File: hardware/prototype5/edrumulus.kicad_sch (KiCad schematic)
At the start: 67 parts, among them J1 Trigger Connector, J2 Raspberry Pi GPIO pins, U1 ESP32-WROOM-32U

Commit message: some more work for prototype 5
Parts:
- removed D18, D19, D20, D22, D23, D24: BAT85, Diode_SMD:D_MiniMELF, symbol Diode:BAT85
- removed R26, R27, R28: 100 kOhm, Resistor_SMD:R_1206_3216Metric_Pad1.30x1.75mm_HandSolder, symbol pspice:R
- removed R30, R31, R32, R34, R35, R36: 22 kOhm, Resistor_SMD:R_1206_3216Metric_Pad1.30x1.75mm_HandSolder, symbol pspice:R
- added D? (x6): BAT85, Diode_SMD:D_MiniMELF, symbol Diode:BAT85
- added R? (x6): 22 kOhm, Resistor_SMD:R_1206_3216Metric_Pad1.30x1.75mm_HandSolder, symbol pspice:R
- added R? (x3): 100 kOhm, Resistor_SMD:R_1206_3216Metric_Pad1.30x1.75mm_HandSolder, symbol pspice:R
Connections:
- net 3V3: now also D?.1 (K), D?.1 (K), D?.1 (K), R?.1, R?.1, R?.1
- net CRASH1-SLEEVE: now also D?.2 (A), D?.2 (A), D?.2 (A), R?.2, R?.2, R?.2
- net GPIO12: now also D?.1 (K), D?.2 (A), R?.1, R?.1, R?.2
- net GPIO15: now also D?.1 (K), D?.2 (A), R?.1, R?.1, R?.2
- net GPIO39: now also D?.1 (K), D?.2 (A), R?.1, R?.1, R?.2
- net TOM1-TIP: now also R?.2
- net TOM2-TIP: now also R?.2
- net TOM3-TIP: now also R?.2
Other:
- moved on the sheet: D1, D10, D11, D12, D13, D14, D15, D16, D17, D2, D21, D25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

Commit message: some more work on prototype 5
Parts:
- removed D? (x2): BAT85, Diode_SMD:D_MiniMELF, symbol Diode:BAT85
- removed R? (x2): 22 kOhm, Resistor_SMD:R_1206_3216Metric_Pad1.30x1.75mm_HandSolder, symbol pspice:R
- removed R?: 100 kOhm, Resistor_SMD:R_1206_3216Metric_Pad1.30x1.75mm_HandSolder, symbol pspice:R
- added C1, C10, C11, C12, C13, C14, C15, C2, C3, C4, C5, C6, C7, C8, C9: 100 nF, symbol Device:C
- added C16: 1 µF, symbol Device:C
- added C17: 22 µF, symbol Device:C_Polarized
- added C18: 10 nF, symbol Device:C
- added C19: 10 µF, symbol Device:C_Polarized
- added D18, D19, D27, D28, D29, D30: BAT85, Diode_SMD:D_MiniMELF, symbol Diode:BAT85
- added R26, R35, R36: 100 kOhm, Resistor_SMD:R_1206_3216Metric_Pad1.30x1.75mm_HandSolder, symbol pspice:R
- added R27, R28, R41, R42, R43, R44: 22 kOhm, Resistor_SMD:R_1206_3216Metric_Pad1.30x1.75mm_HandSolder, symbol pspice:R
- added U2: AMS1117-3.3, Package_TO_SOT_SMD:SOT-223-3_TabPin2, symbol Regulator_Linear:AMS1117-3.3
- added U3: LT1761-3.3, Package_TO_SOT_SMD:TSOT-23-5, symbol Regulator_Linear:LT1761-3.3
- gave numbers to parts that had none: 10
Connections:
- net 3V3: now also C1.2, C10.2, C11.1, C12.2, C13.1, C14.2, C15.1, C18.1, C19.1, C2.1, C3.2, C4.2, C5.1, C6.2, C7.2, C8.1, C9.2, D19.1 (K), D29.1 (K), D30.1 (K), R28.1, R43.1, R44.1, U3.5 (VOUT); no longer U1.2 (VDD)
- net CRASH1-SLEEVE: now also C1.1, C10.1, C11.2, C12.1, C13.2, C14.1, C15.2, C16.2, C17.2, C19.2, C2.2, C3.1, C4.1, C5.2, C6.1, C7.1, C8.2, C9.1, D18.2 (A), D27.2 (A), D28.2 (A), R27.2, R41.2, R42.2, U2.1 (GND), U3.2 (GND)
- net GPIO39: now also D28.1 (K), D30.2 (A), R36.2, R42.1, R44.2
- net TOM1-TIP: now also R36.1
- net TOM1-RING: now reaches J1.15 (P15)
- net TOM1-RING: now also R35.1
- net RIDE-BELL-TIP: now reaches J1.25 (P25)
- net RIDE-BELL-TIP: now also R26.1
- net GPIO2: now reaches U1.24 (IO2)
- net GPIO2: now also D18.1 (K), D19.2 (A), R26.2, R27.1, R28.2
- net GPIO4: now reaches U1.26 (IO4)
- net GPIO4: now also D27.1 (K), D29.2 (A), R35.2, R41.1, R43.2
- net ESP-VIN renamed RASPI-VIN
- net RASPI-VIN: now also C16.1, U2.3 (VI), U3.1 (VIN), U3.3 (~{SHDN})
- new net: C18.2, U3.4 (BYP)
- new net ESP32-3V3: C17.1, U1.2 (VDD), U2.2 (VO)
- no-connect marks 34 -> 38
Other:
- note added: "TODO ESP 32 enable TODO Board LED"
- title: Edrumulus Prototype 4 (ESP32) -> Edrumulus Prototype 5 (ESP32)
- moved on the sheet: D17, D20, D21, D22, D23, D24, D25, D26, J1, J2, R25, R29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

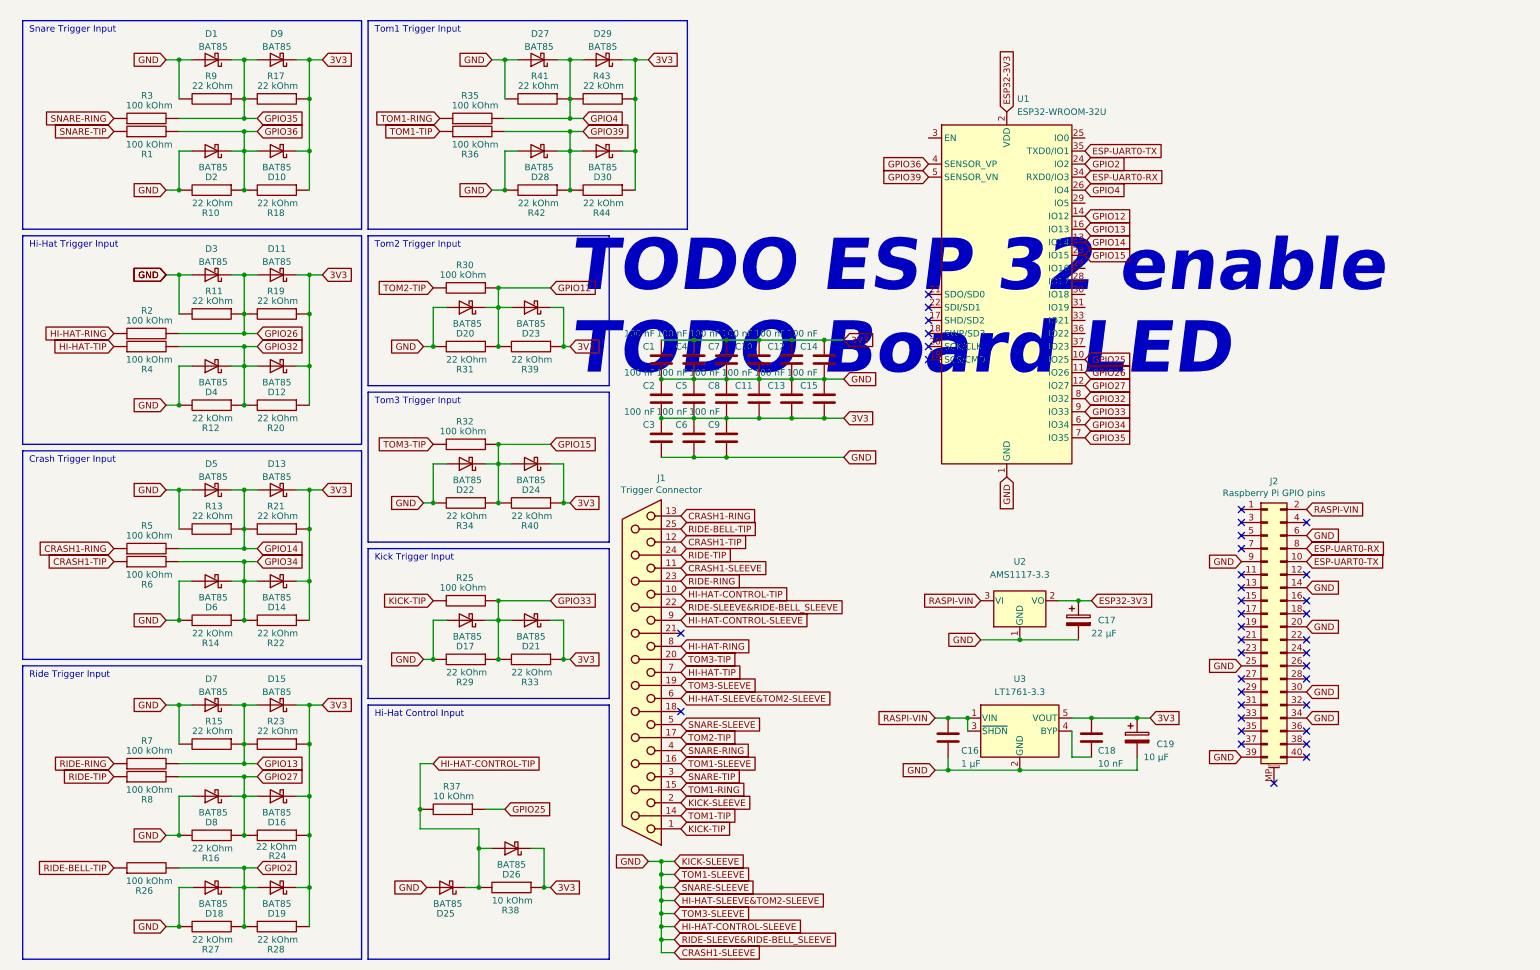
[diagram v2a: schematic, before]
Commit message: added enable and LED
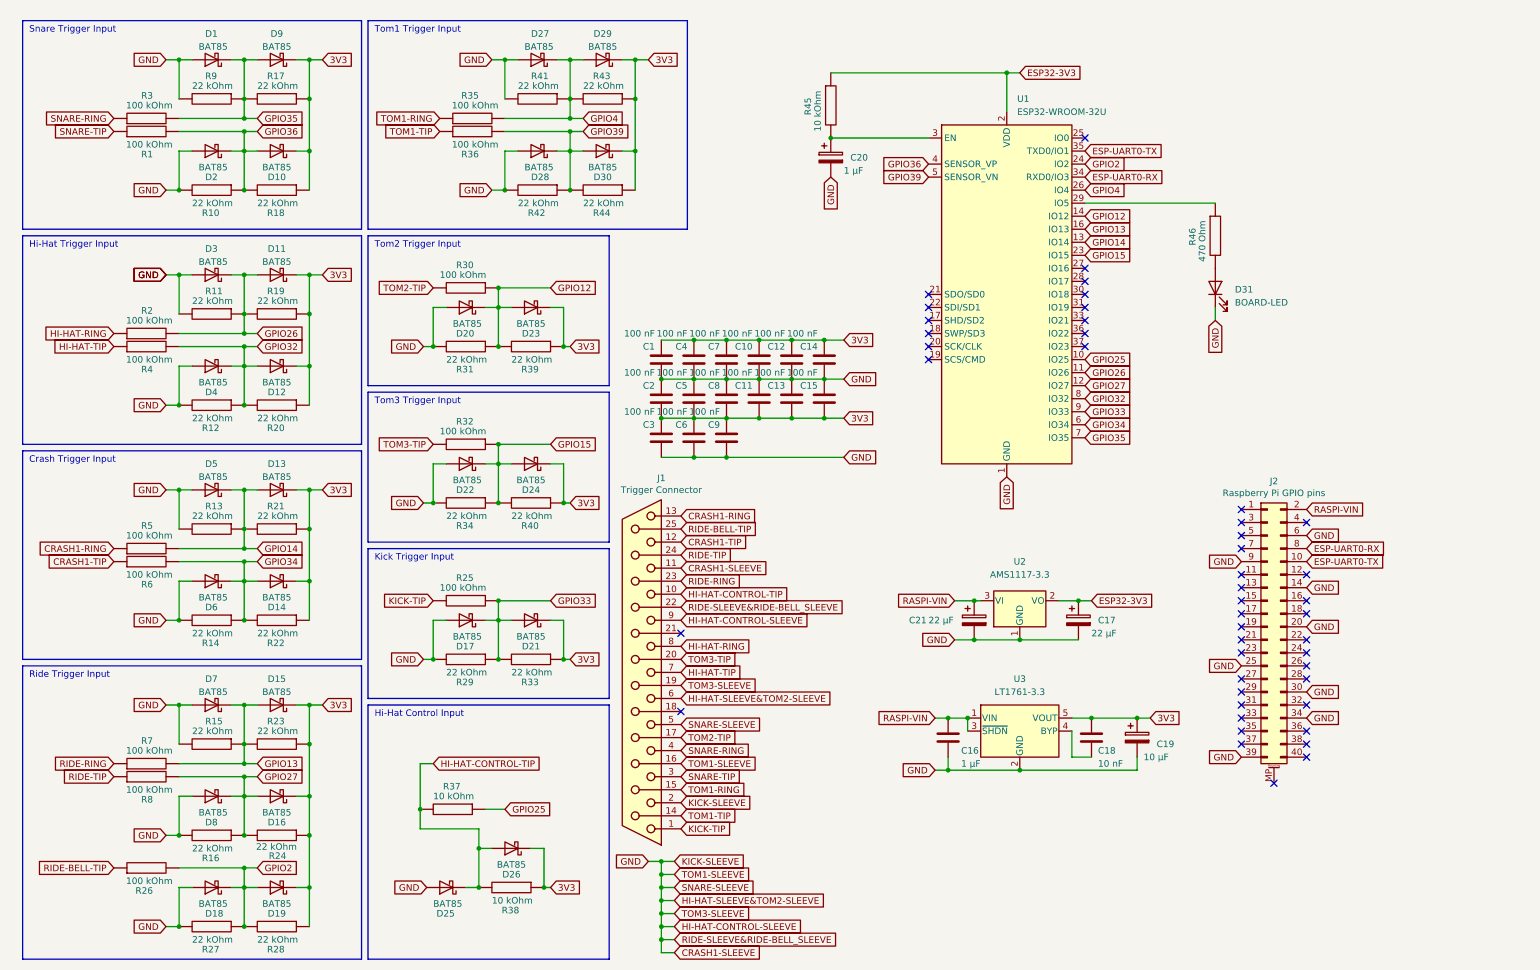
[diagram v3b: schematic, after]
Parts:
- added C20: 1 µF, symbol Device:C_Polarized
- added C21: 22 µF, symbol Device:C_Polarized
- added D31: BOARD-LED, symbol Device:LED
- added R45: 10 kOhm, Resistor_SMD:R_1206_3216Metric_Pad1.30x1.75mm_HandSolder, symbol pspice:R
- added R46: 470 Ohm, Resistor_SMD:R_1206_3216Metric_Pad1.30x1.75mm_HandSolder, symbol pspice:R
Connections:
- net CRASH1-SLEEVE: now also C20.2, C21.2, D31.1 (K)
- net ESP32-3V3: now also R45.1
- net RASPI-VIN: now also C21.1
- net at U1.29 (IO5): now also R46.1
- net at U1.3 (EN): now also C20.1, R45.2
- new net: D31.2 (A), R46.2
- no-connect marks 38 -> 46
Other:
- note removed: "TODO ESP 32 enable TODO Board LED"

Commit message: some layout cleanup
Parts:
- C1, C10, C11, C12, C13, C14, C15, C16, C17, C18, C19, C2, C20, C21, C3, C4, C5, C6, C7, C8, C9: footprint (none) -> Capacitor_SMD:C_1206_3216Metric_Pad1.33x1.80mm_HandSolder
- D31: footprint (none) -> LED_SMD:LED_0603_1608Metric

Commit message: some more prototype 5 development
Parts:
- J1: footprint Connector_Dsub:DSUB-25_Female_Vertical_P2.77x2.84mm -> Connector_Dsub:DSUB-25_Female_Horizontal_P2.77x2.84mm_EdgePinOffset7.70mm_Housed_MountingHolesOffset9.12mm
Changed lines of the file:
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@@
     (property "Reference" "J1" (id 0) (at 138.43 103.0986 0))
     (property "Value" "Trigger Connector" (id 1) (at 138.43 105.41 0))
-    (property "Footprint" "Connector_Dsub:DSUB-25_Female_Vertical_P2.77x2.84mm" (id 2) (at 134.62 140.97 0)
+    (property "Footprint" "Connector_Dsub:DSUB-25_Female_Horizontal_P2.77x2.84mm_EdgePinOffset7.70mm_Housed_MountingHolesOffset9.12mm" (id 2) (at 134.62 140.97 0)
       (effects (font (size 1.27 1.27)) hide)
     )
@@
     )
     (path "/00000000-0000-0000-0000-000062d47c5a"
-      (reference "J1") (unit 1) (value "Trigger Connector") (footprint "Connector_Dsub:DSUB-25_Female_Vertical_P2.77x2.84mm")
+      (reference "J1") (unit 1) (value "Trigger Connector") (footprint "Connector_Dsub:DSUB-25_Female_Horizontal_P2.77x2.84mm_EdgePinOffset7.70mm_Housed_MountingHolesOffset9.12mm")
     )
     (path "/00000000-0000-0000-0000-000062d10684"

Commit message: prototype 5 component placement
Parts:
- removed C11, C12, C13, C5, C6, C7, C8, C9: 100 nF, Capacitor_SMD:C_1206_3216Metric_Pad1.33x1.80mm_HandSolder, symbol Device:C
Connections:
- net 3V3: now also C15.2, C2.2; no longer C15.1, C2.1
- net CRASH1-SLEEVE: now also C15.1, C2.1; no longer C15.2, C2.2
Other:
- moved on the sheet: C1, C10, C14, C15, C2, C3, C4

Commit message: connect GPIOs for boot/enable, some more routing for prototype 5
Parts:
- removed C20: 1 µF, Capacitor_SMD:C_1206_3216Metric_Pad1.33x1.80mm_HandSolder, symbol Device:C_Polarized
- added R47: 10 kOhm, Resistor_SMD:R_1206_3216Metric_Pad1.30x1.75mm_HandSolder, symbol pspice:R
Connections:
- net CRASH1-SLEEVE: now also R45.1
- net ESP32-3V3: now also R47.1; no longer R45.1
- net PI-GPIO9: now reaches J2.21 (Pin_21)
- net PI-GPIO9: now also R45.2, U1.3 (EN)
- net PI-GPIO4: now reaches J2.7 (Pin_7)
- net PI-GPIO4: now also U1.25 (IO0), R47.2
- no-connect marks 46 -> 43
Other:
- moved on the sheet: R45

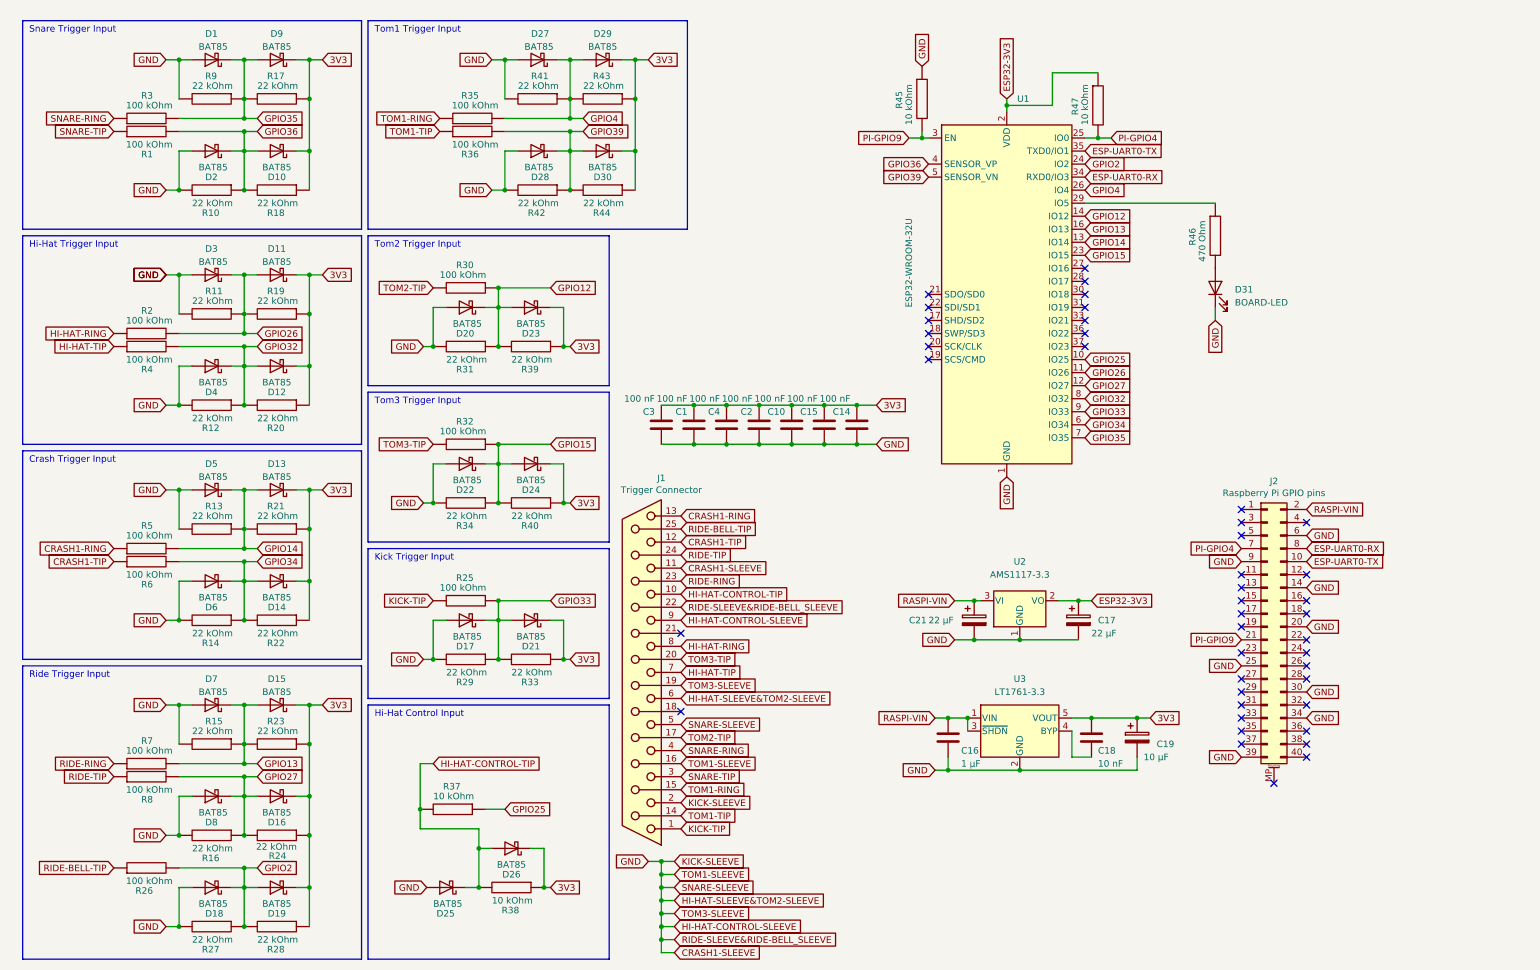
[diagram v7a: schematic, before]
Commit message: new linear controller for SDB bias
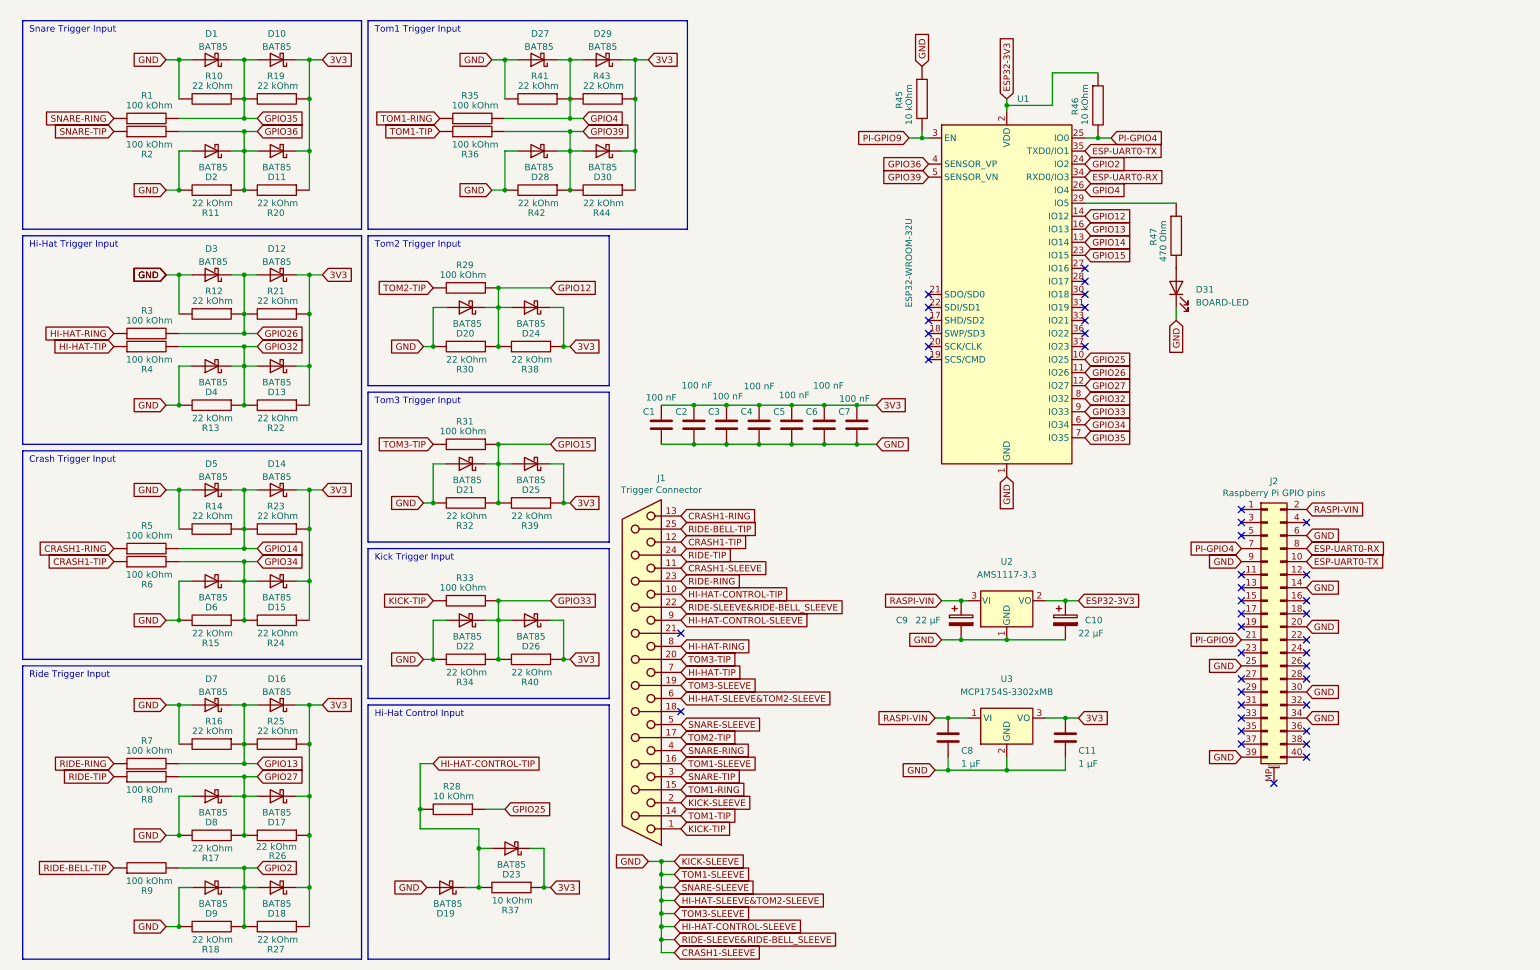
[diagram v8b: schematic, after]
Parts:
- removed C18: 10 nF, Capacitor_SMD:C_1206_3216Metric_Pad1.33x1.80mm_HandSolder, symbol Device:C
- removed C19: 10 µF, Capacitor_SMD:C_1206_3216Metric_Pad1.33x1.80mm_HandSolder, symbol Device:C_Polarized
- removed U3: LT1761-3.3, Package_TO_SOT_SMD:TSOT-23-5, symbol Regulator_Linear:LT1761-3.3
- added C11: 1 µF, Capacitor_SMD:C_1206_3216Metric_Pad1.33x1.80mm_HandSolder, symbol Device:C
- added U3: MCP1754S-3302xMB, Package_TO_SOT_SMD:SOT-89-3, symbol Regulator_Linear:MCP1754S-3302xMB
- renumbered C3 to C1, C17 to C10, C1 to C2, C4 to C3, C2 to C4, C10 to C5, C15 to C6, C14 to C7, C16 to C8, C21 to C9, D9 to D10, D10 to D11, D11 to D12, D12 to D13, D13 to D14, D14 to D15, D15 to D16, D16 to D17, D19 to D18, D25 to D19, D22 to D21, D17 to D22, D26 to D23, D23 to D24, D24 to D25, D21 to D26, D18 to D9, R3 to R1, R9 to R10, R10 to R11, R11 to R12, R12 to R13, R13 to R14, R14 to R15, R15 to R16, R16 to R17, R27 to R18, R17 to R19, R1 to R2, R18 to R20, R19 to R21, R20 to R22, R21 to R23, R22 to R24, R23 to R25, R24 to R26, R28 to R27, R37 to R28, R30 to R29, R2 to R3, R31 to R30, R32 to R31, R34 to R32, R25 to R33, R29 to R34, R38 to R37, R39 to R38, R40 to R39, R33 to R40, R47 to R46, R46 to R47, R26 to R9
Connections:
- net 3V3: now also C11.1, U3.3 (VO)
- net CRASH1-SLEEVE: now also C11.2, U3.2 (GND)
- net RASPI-VIN: now also U3.1 (VI)
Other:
- moved on the sheet: C10, C9, D31, R47, U2
